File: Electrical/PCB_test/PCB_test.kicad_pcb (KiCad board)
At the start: 2 copper layers, 37 parts, among them J1 Screw_Terminal_01x02

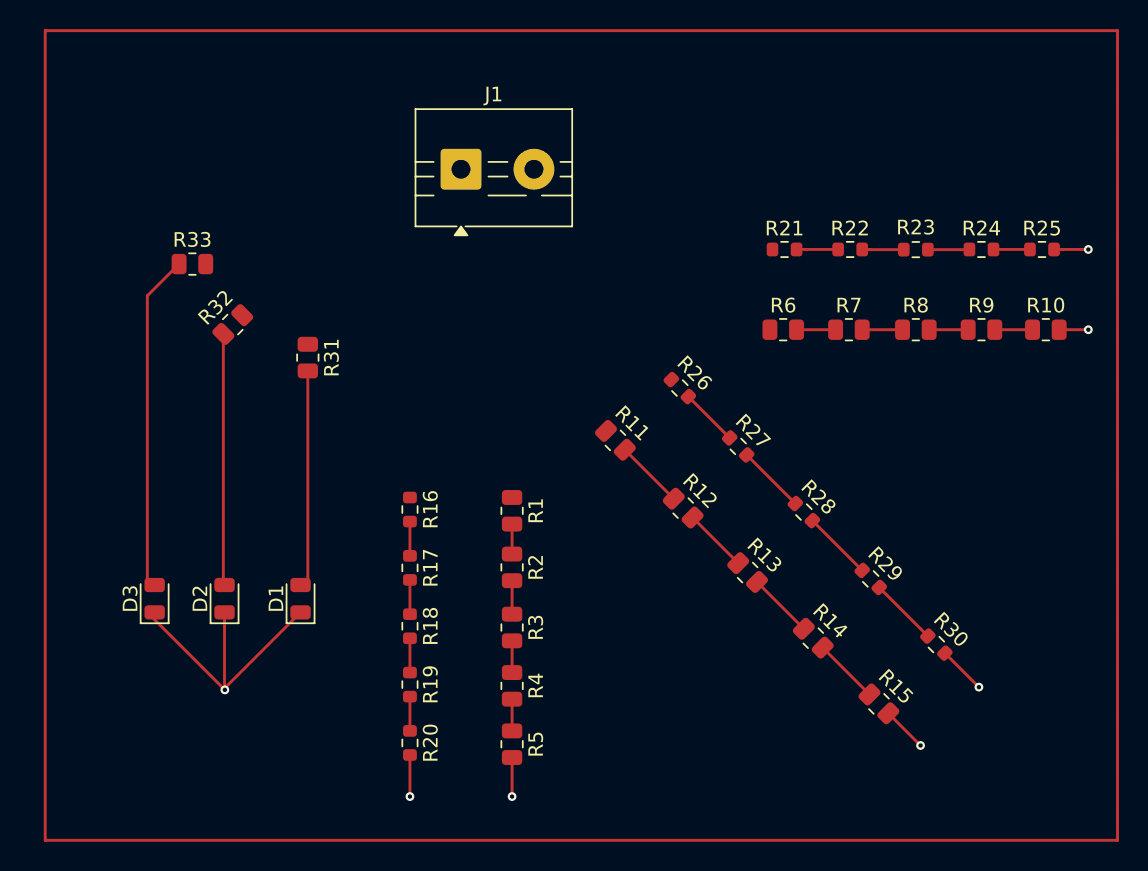
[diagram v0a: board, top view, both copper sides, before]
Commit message: Calibration and mounting hole added to test PCB
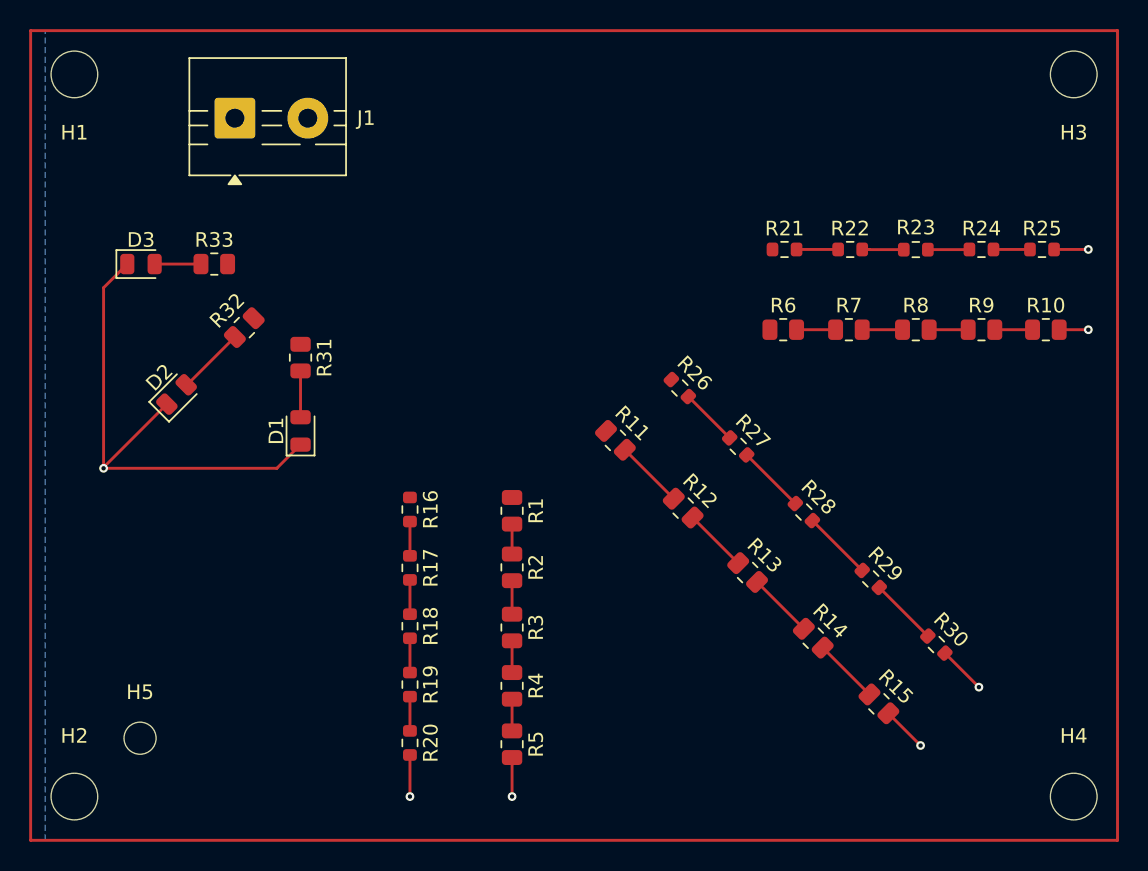
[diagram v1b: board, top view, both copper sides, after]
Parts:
- added H1: MountingHole, MountingHole:MountingHole_3.2mm_M3, F.Cu at (46.5, 33.5)
- added H2: MountingHole, MountingHole:MountingHole_3.2mm_M3, F.Cu at (46.5, 83.0)
- added H3: MountingHole, MountingHole:MountingHole_3.2mm_M3, F.Cu at (115.0, 33.5)
- added H4: MountingHole, MountingHole:MountingHole_3.2mm_M3, F.Cu at (115.0, 83.0)
- added H5: MountingHole, MountingHole:MountingHole_2.2mm_M2, F.Cu at (51.0, 79.0)
- moved D3 23.0 mm to (51.1, 46.5), turned to 0 degrees
- moved J1 15.9 mm to (57.5, 36.5)
- moved D2 14.4 mm to (53.5, 55.4), turned to 45 degrees
- moved D1 11.5 mm to (62.0, 57.9)
- moved R33 1.50 mm to (56.1, 46.5)
- moved R32 0.82 mm to (58.1, 50.9)
- moved R31 0.50 mm to (62.0, 52.9)
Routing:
- net Net-(D3-A): track 22.9 -> 3.17 mm
- net GND: track 37.1 -> 51.3 mm
- net Net-(D2-A): track 17.3 -> 4.69 mm
- net Net-(D1-A): track 14.7 -> 3.17 mm

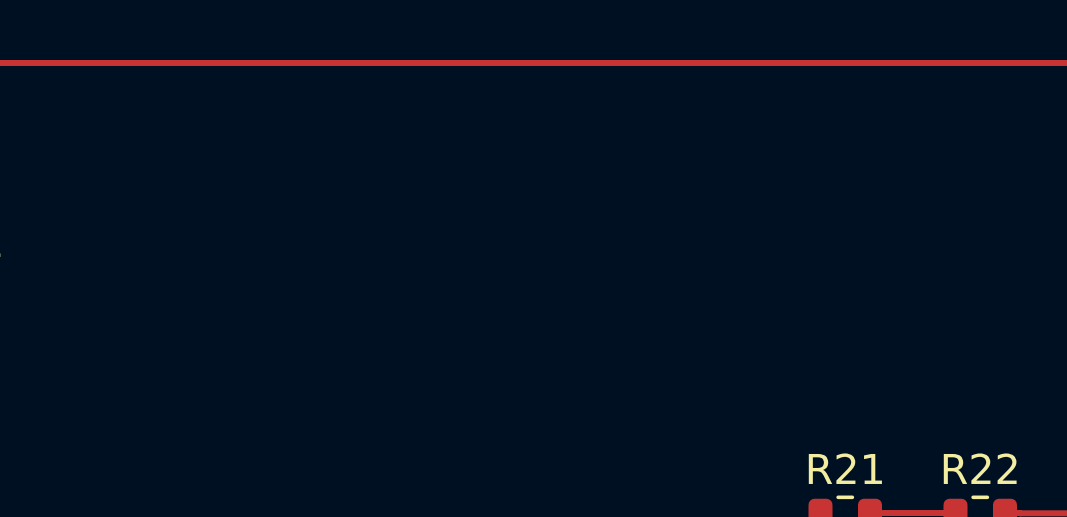
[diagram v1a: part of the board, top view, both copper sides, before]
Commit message: Name and logo added to test PCB
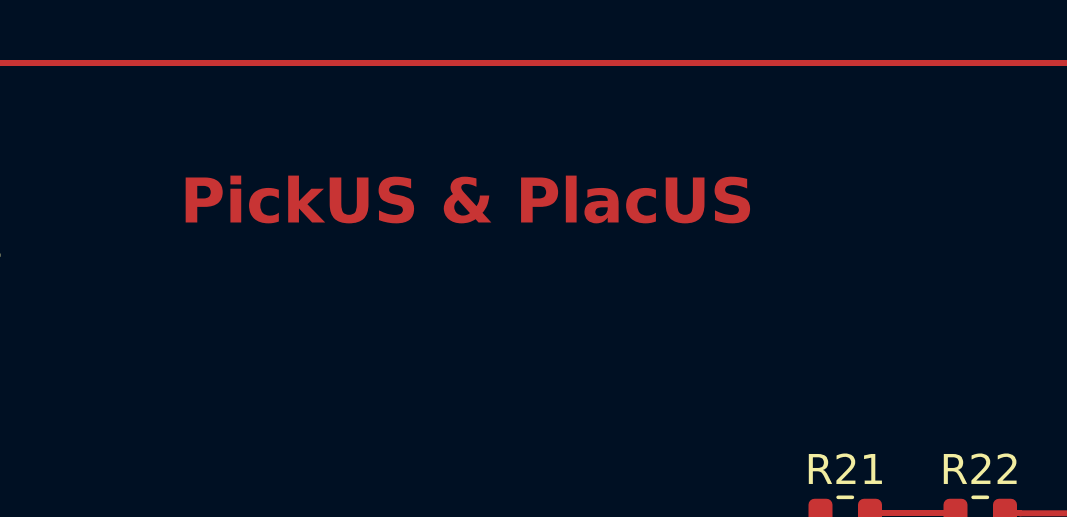
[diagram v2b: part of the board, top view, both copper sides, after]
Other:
- board text added: "PickUS & PlacUS"
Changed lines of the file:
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@@
 		(layer "F.Cu")
+	)
+	(gr_text "PickUS & PlacUS"
+		(at 73 36 0)
+		(layer "F.Cu")
+		(effects
+			(font
+				(size 1.5 1.5)
+				(thickness 0.3)
+				(bold yes)
+			)
+			(justify left bottom)
+		)
 	)
 	(segment

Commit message: forgot to save file lmao
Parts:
- added G***: LOGO, LOGO, F.Cu at (80.5, 44.5)
